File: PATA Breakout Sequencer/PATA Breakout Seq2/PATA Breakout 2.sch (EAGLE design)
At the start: 57 parts, among them IC1 74HC165N, IC2 74HC165N, IC3 74HC165N, IC4 74HC165N, IC5 74HC165N

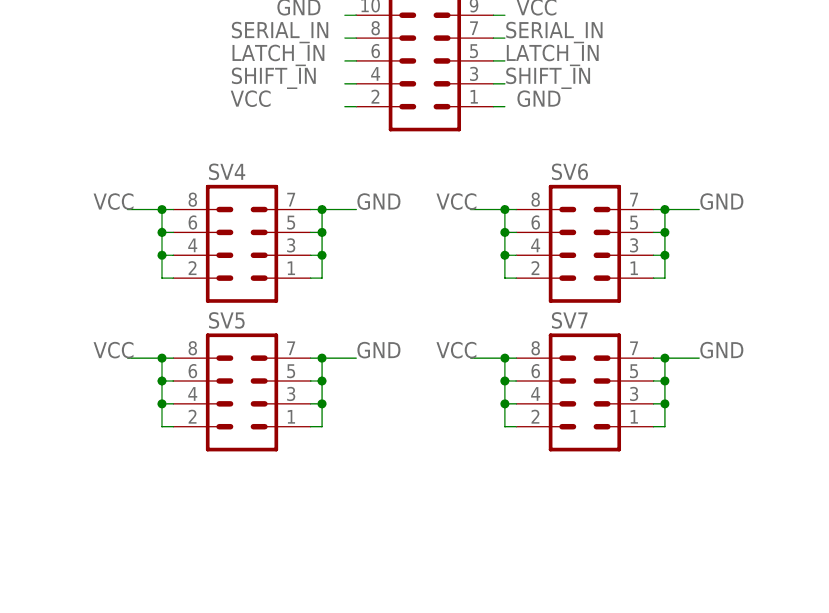
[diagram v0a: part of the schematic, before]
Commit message: Finished top board - ran DRC
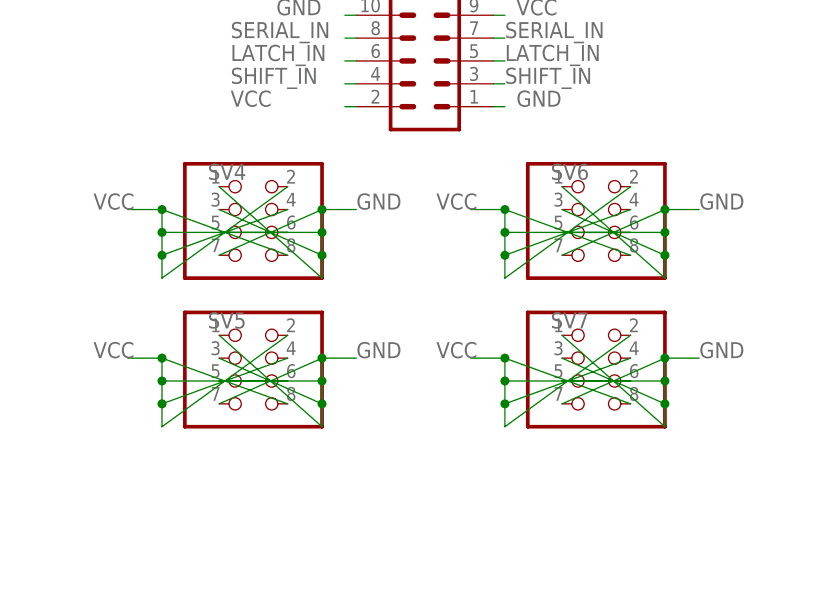
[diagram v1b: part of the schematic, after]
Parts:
- SV4, SV5, SV6, SV7: device con-lstb:MA04-2 -> pinhead:PINHD-2X4
